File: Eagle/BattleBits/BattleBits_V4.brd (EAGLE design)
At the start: 140 x 140 mm, 105 parts, among them IC1 4001N, IC10 REG1117, IC11 LM2901D, IC12 LM2901D, IC2 ULN2004AD, IC3 4001N, IC4 ULN2004AD, IC5 ULN2004AD, IC6 ULN2004AD, IC7 ULN2004AD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

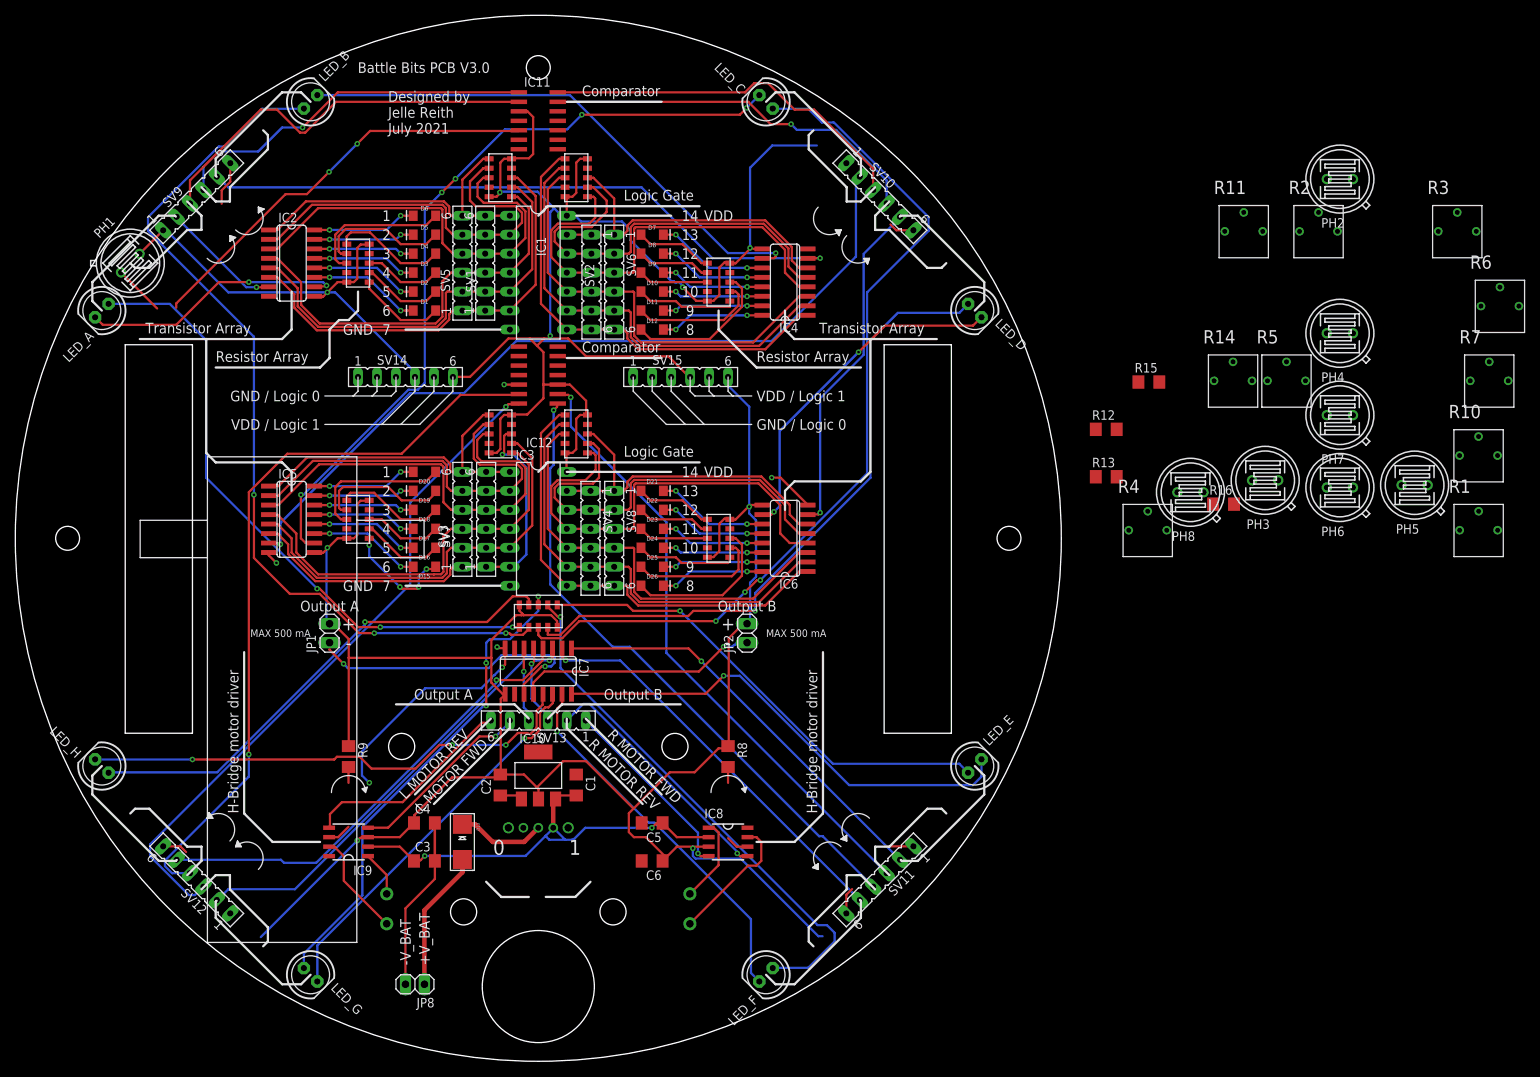
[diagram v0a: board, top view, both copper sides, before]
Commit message: silkscreen added
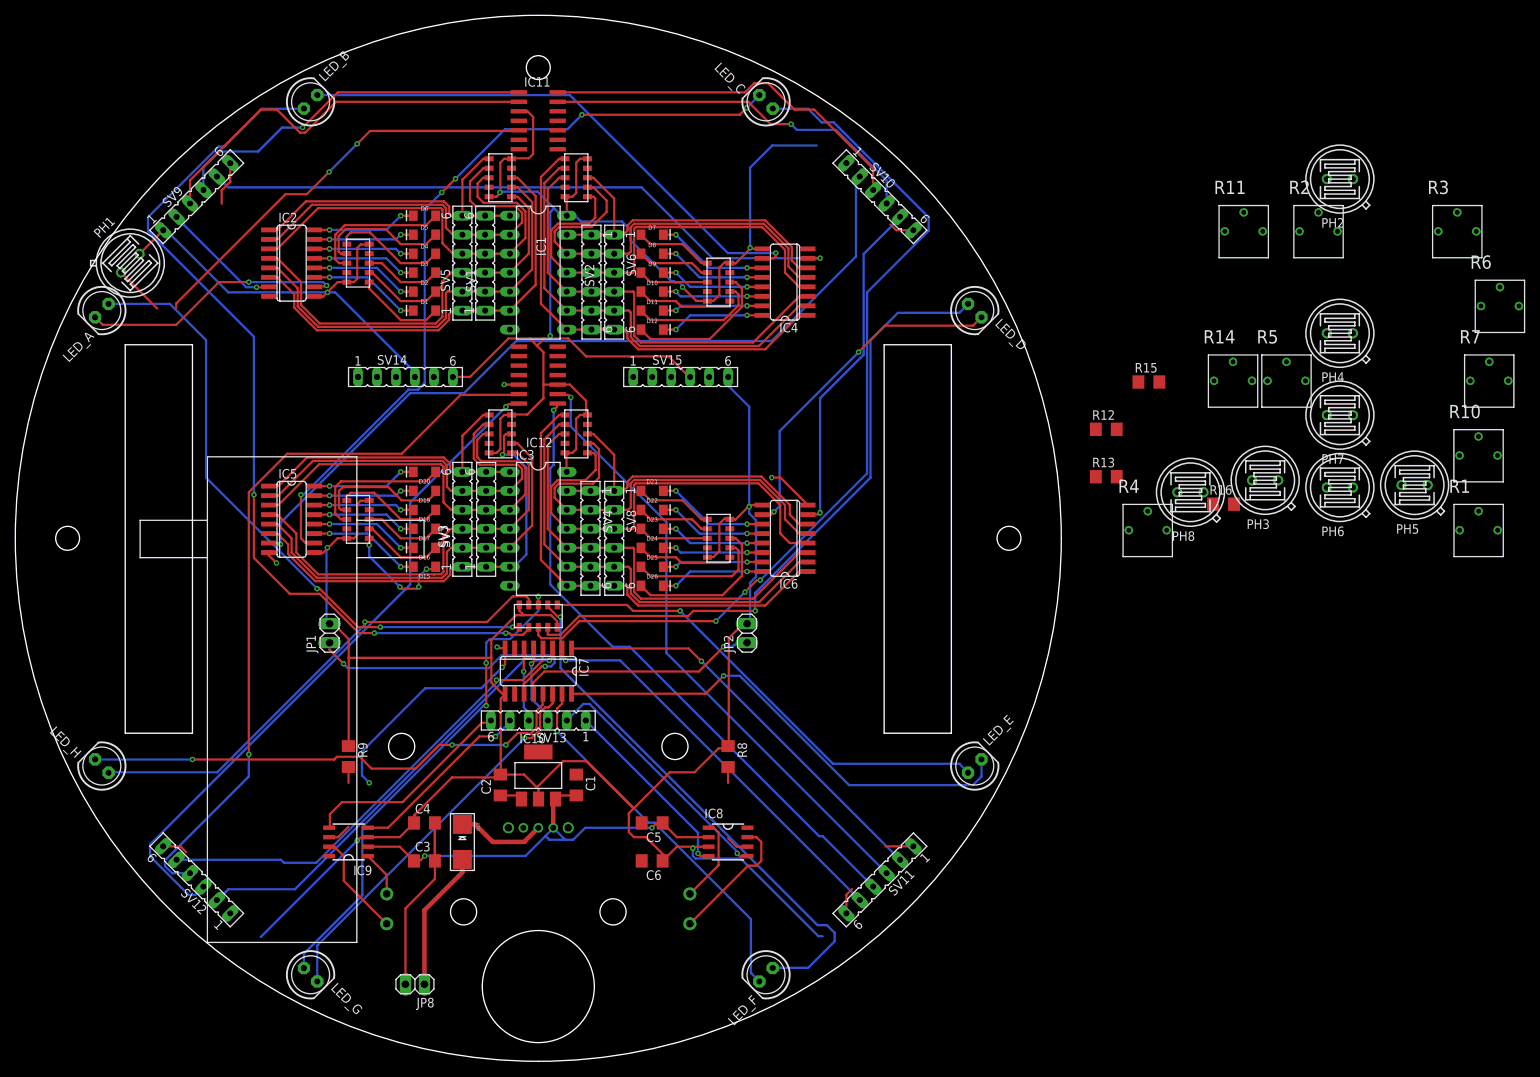
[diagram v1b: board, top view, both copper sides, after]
